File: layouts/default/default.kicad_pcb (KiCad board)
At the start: 2 copper layers, 21 parts

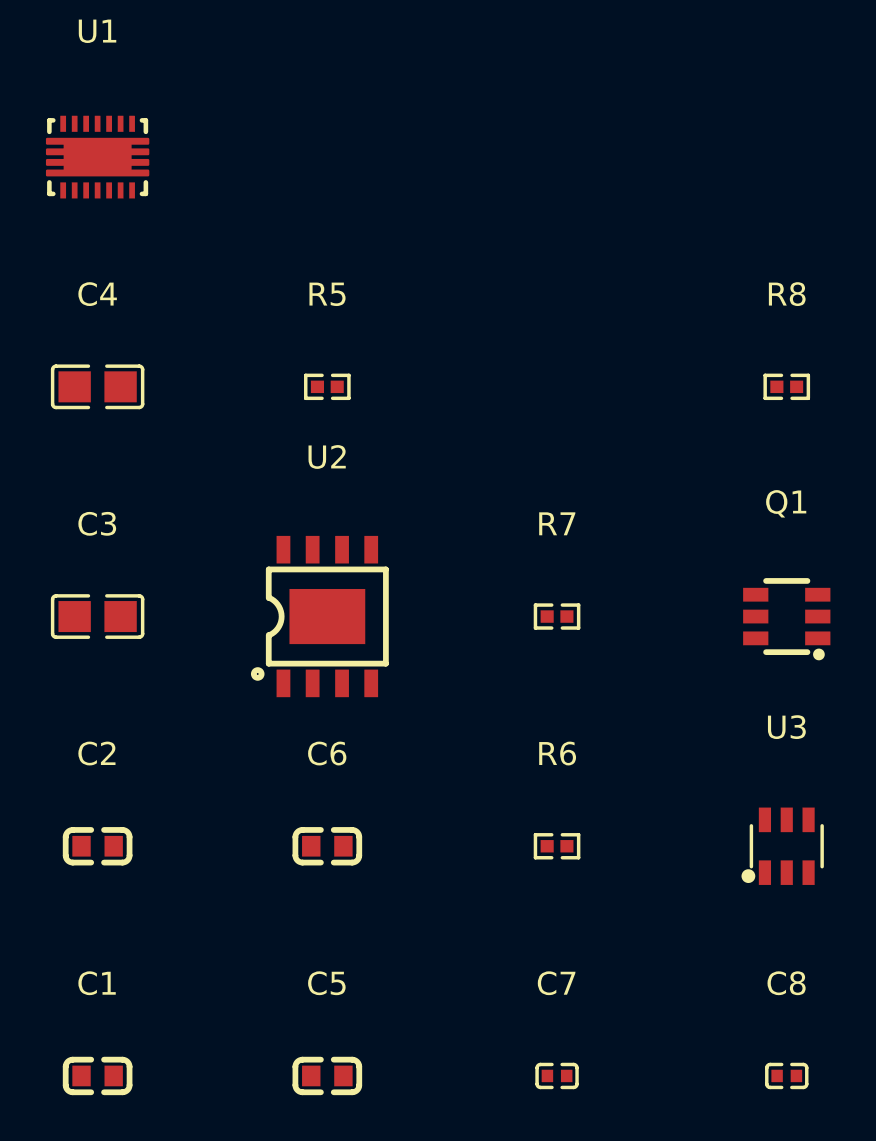
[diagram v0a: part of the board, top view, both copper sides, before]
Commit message: Upgrade to atopile v0.14.0 (Python 3.14), fix pin names
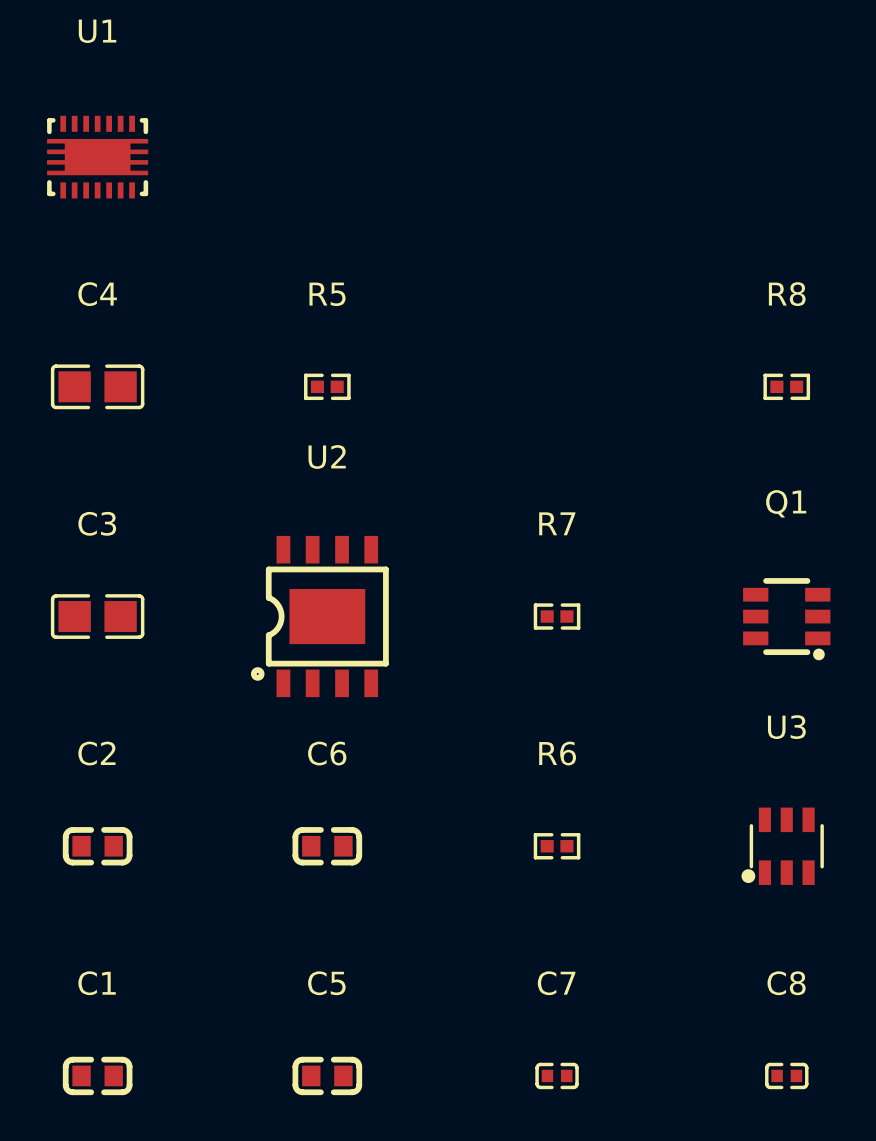
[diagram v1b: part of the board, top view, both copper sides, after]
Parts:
- C1, C2: value 10µF ±10% 10V X5R -> 0F
- C3, C4: value 22µF ±20% 25V X5R -> 0F
- C5, C6: value 4.7µF ±10% 16V X5R -> 0F
- C7, C8: value 100nF ±10% 16V X7R -> 0F
- L1: value 2.2µH ±20% 3A 55mΩ -> L 0H
- R1, R4: value 100kΩ ±1% 62.5mW -> 100000Ω
- R2: value 110kΩ ±1% 62.5mW -> 110000Ω
- R3, R6, R7: value 1MΩ ±1% 62.5mW -> 1000000Ω
- R5: value 2kΩ ±1% 62.5mW -> 2000Ω
- R8: value 100Ω ±1% 62.5mW -> 100Ω
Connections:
- net D12 renamed 2
- net L1 renamed 8
- net L2 renamed 6
- net bat_neg renamed c_prot-power-lv
- net gnd renamed lv
- net v5_pi renamed c_vout2-power-hv
- net vbat renamed hv
- net vbat_sns renamed c_adc-power-hv
- net vusb renamed c_in-power-hv

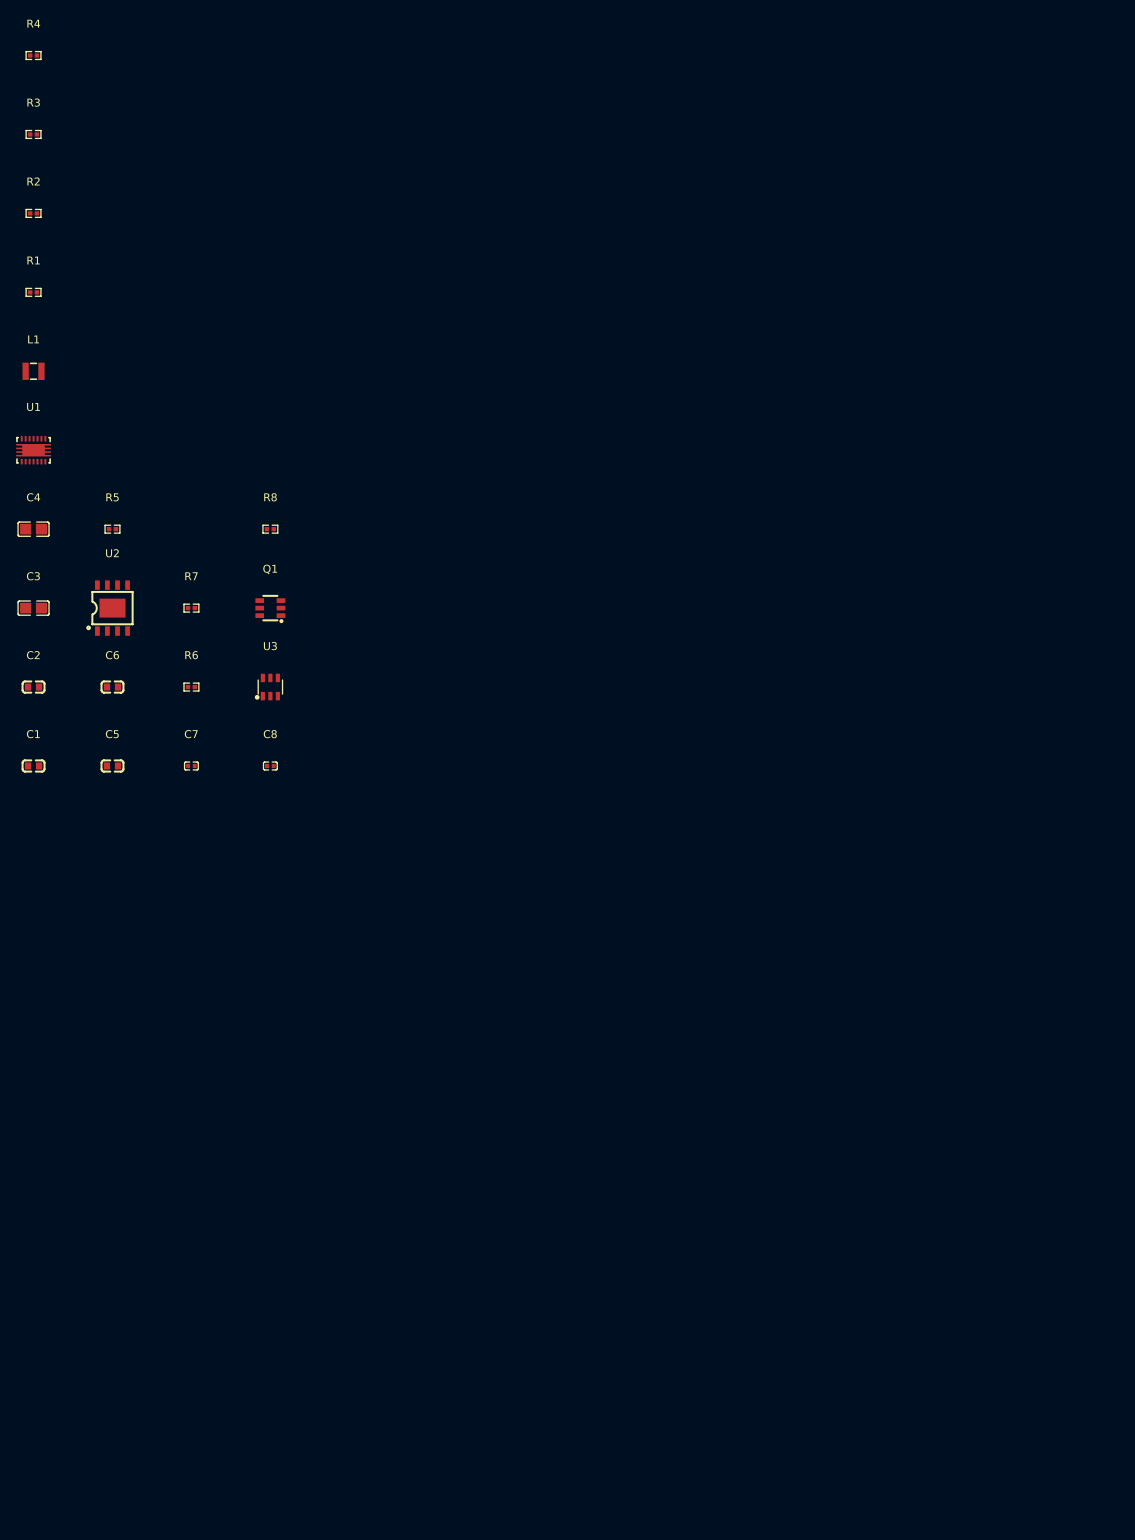
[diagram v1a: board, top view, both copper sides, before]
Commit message: Rearrange PCB layout: group by functional block (buck-boost/charger/protection/monitor), add 39.5x16.5mm board outline
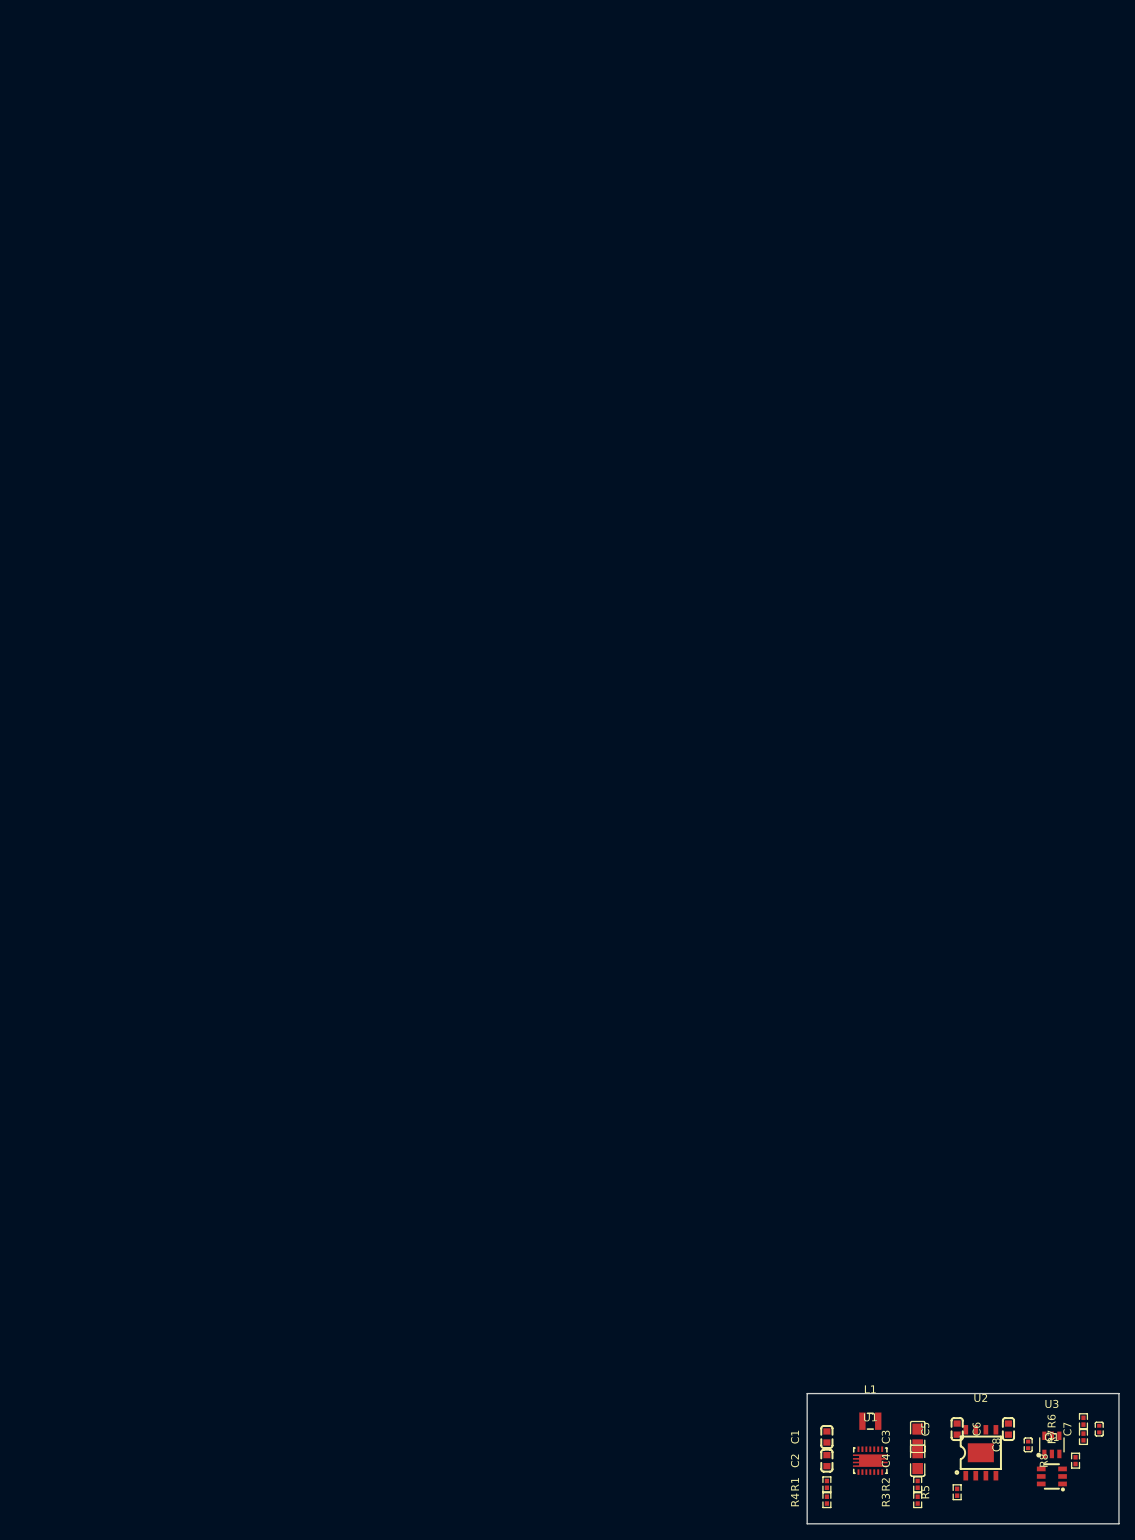
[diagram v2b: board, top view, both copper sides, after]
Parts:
- moved R4 208.8 mm to (100.5, 93.0), turned to 90 degrees
- moved R3 206.1 mm to (112.0, 93.0), turned to 90 degrees
- moved R2 196.1 mm to (112.0, 91.0), turned to 90 degrees
- moved R1 181.4 mm to (100.5, 91.0), turned to 90 degrees
- moved L1 170.1 mm to (106.0, 83.0)
- moved U1 166.2 mm to (106.0, 88.0)
- moved C4 162.7 mm to (112.0, 88.0), turned to 90 degrees
- moved R5 162.3 mm to (117.0, 92.0), turned to 90 degrees
- moved R8 156.0 mm to (132.0, 88.0), turned to 90 degrees
- moved R7 154.3 mm to (133.0, 85.0), turned to 90 degrees
- moved C3 153.5 mm to (112.0, 85.0), turned to 90 degrees
- moved U2 153.5 mm to (120.0, 87.0)
- moved Q1 148.0 mm to (129.0, 90.0)
- moved C6 147.4 mm to (123.5, 84.0), turned to 90 degrees
- moved R6 146.3 mm to (133.0, 83.0), turned to 90 degrees
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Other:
- board outline added: 39.5 x 16.5 mm
